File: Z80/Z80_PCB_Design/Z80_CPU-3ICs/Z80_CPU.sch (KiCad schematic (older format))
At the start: 47 parts, among them J1 USB_B, J2 Conn_01x12, J3 Conn_01x12, J4 Conn_01x02, U1 Z80CPU, U2 AS6C4008, U3 4.9152 MHz, U4 CY8C5267AXI-LP051, U5 MCP23017_SP, Y1 32.768KHz

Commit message: Added SPI pinout
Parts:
- MTG1, MTG2, MTG3, MTG4: symbol LandBoards:MTG_HOLE -> Z80_CPU-rescue:MTG_HOLE-LandBoards
- U3: symbol LandBoards_Semis:OSC -> Z80_CPU-rescue:OSC-LandBoards_Semis
- U4: symbol LandBoards_Semis:CY8C5888AXI-LP096 -> Z80_CPU-rescue:CY8C5888AXI-LP096-LandBoards_Semis
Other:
- note added: "AUDIO CONNECTOR/\nLOW PASS FILTER"
- note added: "TX (MISO)\nRX (MOSI)\nRTS (SCK)\nCTS (SS)"
- note removed: "AUDIO CONNECTOR"
- moved on the sheet: H3, J1, J2, J3, U1, U2, U5

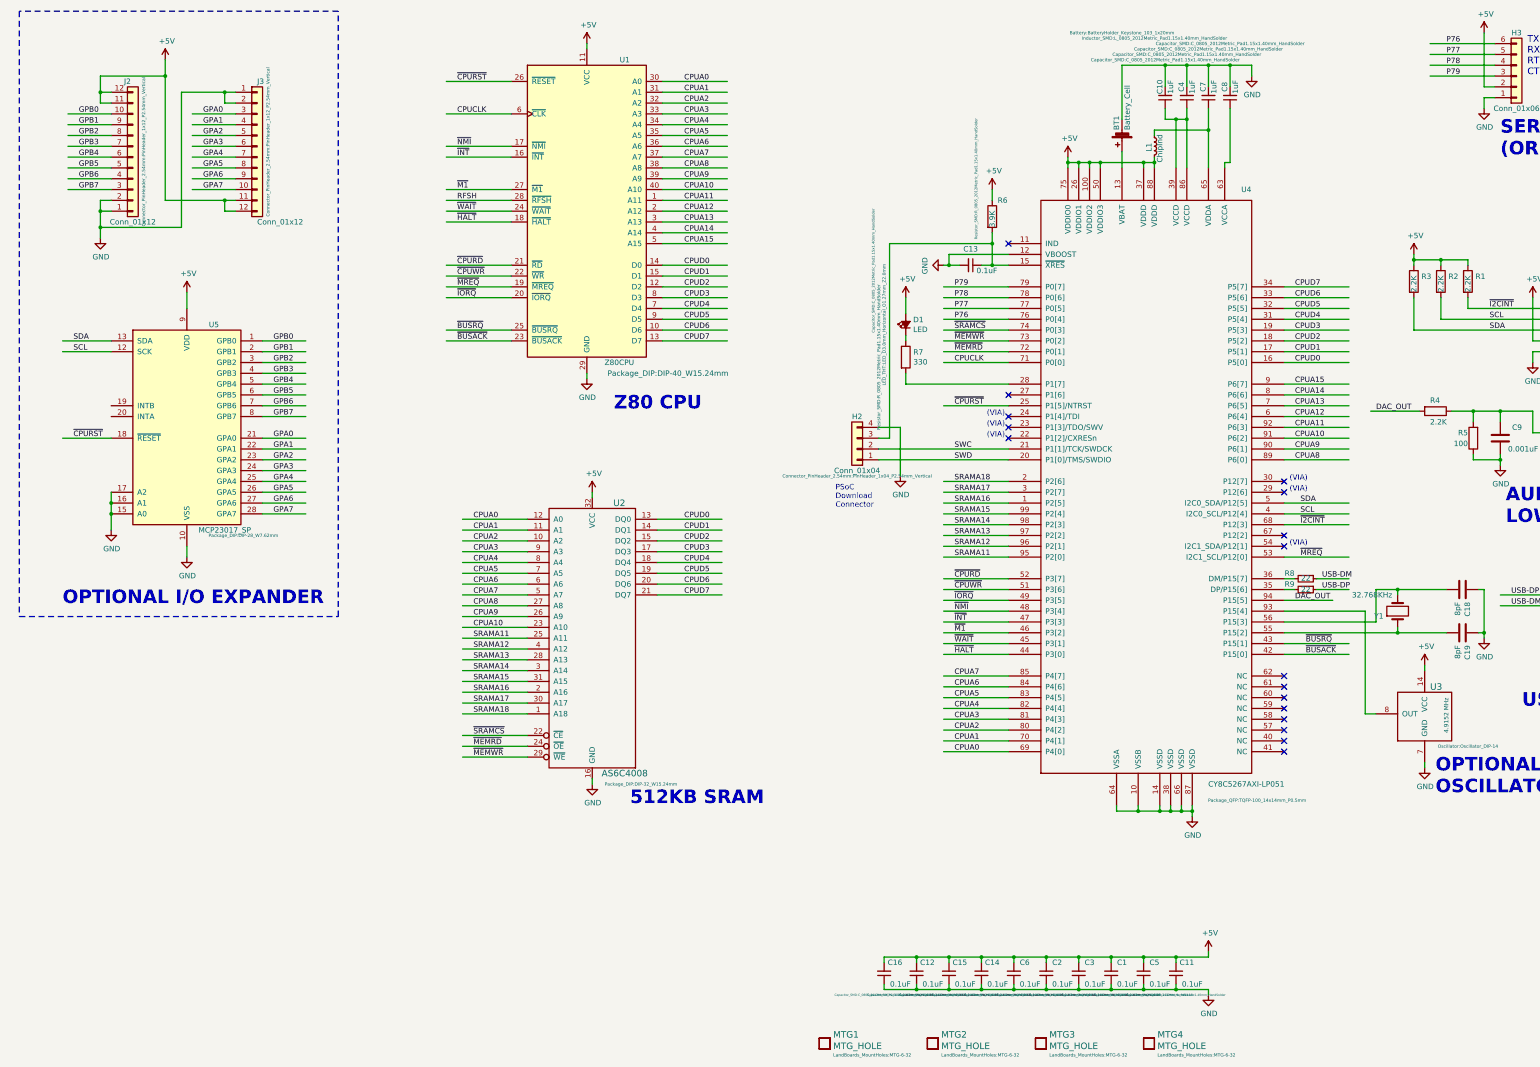
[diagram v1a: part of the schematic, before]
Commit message: Grand Piano on DAC8 output
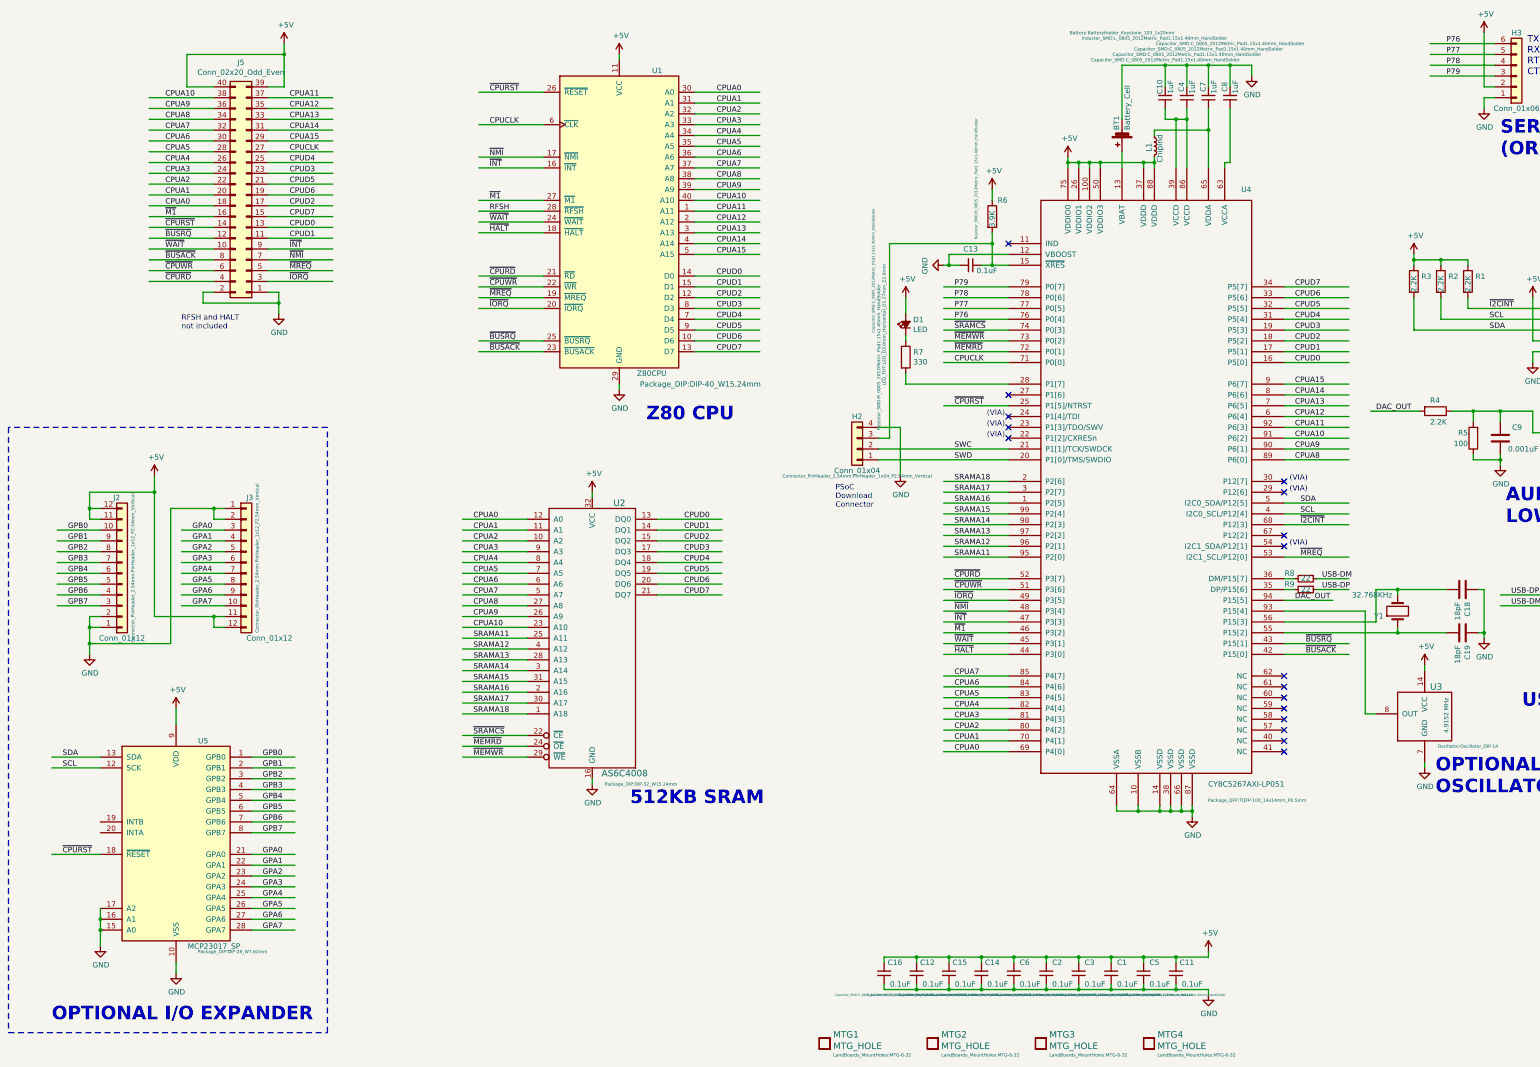
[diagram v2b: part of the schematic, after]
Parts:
- added J5: Conn_02x20_Odd_Even, Connector_PinHeader_2.54mm:PinHeader_2x20_P2.54mm_Horizontal, symbol Connector_Generic:Conn_02x20_Odd_Even
- C18, C19: value 8pF -> 18pF
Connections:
- wire segments 366 -> 414
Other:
- note added: "RFSH and HALT\nnot included"
- moved on the sheet: J2, J3, U1, U5

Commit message: pio init stuck z80
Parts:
- R1: value 2.2K -> 10K
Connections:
- wire segments 414 -> 418
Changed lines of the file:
@@
 P 14150 3300
 F 0 "R1" H 14220 3346 50  0000 L CNN
-F 1 "2.2K" V 14150 3200 50  0000 L CNN
+F 1 "10K" V 14150 3200 50  0000 L CNN
 F 2 "Resistor_SMD:R_0805_2012Metric_Pad1.15x1.40mm_HandSolder" V 14080 3300 50  0001 C CNN
 F 3 "~" H 14150 3300 50  0001 C CNN
@@
 Wire Wire Line
 	1950 1700 2550 1700
+Text Label 1150 8400 0    50   ~ 0
+~I2CINT
+Wire Wire Line
+	1050 8400 1450 8400
+Wire Wire Line
+	1450 8400 1450 8300
+Wire Wire Line
+	1450 8300 1500 8300
+Connection ~ 1450 8400
+Wire Wire Line
+	1450 8400 1500 8400
 $EndSCHEMATC

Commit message: remove cpu reset from expansion mcp23017
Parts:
- added R10: 10K, Resistor_SMD:R_0805_2012Metric_Pad1.15x1.40mm_HandSolder, symbol Device:R
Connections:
- wire segments 418 -> 420
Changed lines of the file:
@@
 	1    0    0    -1
 $EndComp
-Text Label 1150 8600 0    50   ~ 0
-~CPURST
-Wire Wire Line
-	1050 8600 1500 8600
+Wire Wire Line
+	850  8600 1500 8600
 Wire Wire Line
 	1500 9100 1500 9200
@@
 Wire Wire Line
 	1450 8400 1500 8400
+$Comp
+L Device:R R10
+U 1 1 5DC2CA82
+P 850 8350
+F 0 "R10" H 900 8500 50  0000 L CNN
+F 1 "10K" V 850 8250 50  0000 L CNN
+F 2 "Resistor_SMD:R_0805_2012Metric_Pad1.15x1.40mm_HandSolder" V 700 8700 25  0000 C CNN
+F 3 "~" H 850 8350 50  0001 C CNN
+	1    850  8350
+	1    0    0    -1
+$EndComp
+$Comp
+L power:+5V #PWR04
+U 1 1 5DC6B53D
+P 850 8050
+F 0 "#PWR04" H 850 7900 50  0001 C CNN
+F 1 "+5V" H 865 8223 50  0000 C CNN
+F 2 "" H 850 8050 50  0001 C CNN
+F 3 "" H 850 8050 50  0001 C CNN
+	1    850  8050
+	1    0    0    -1
+$EndComp
+Wire Wire Line
+	850  8050 850  8200
+Wire Wire Line
+	850  8500 850  8600
 $EndSCHEMATC

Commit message: Add 4 pin connector to spare PSoC pins
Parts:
- added H4: Conn_01x06, Connector_PinHeader_2.54mm:PinHeader_1x06_P2.54mm_Vertical, symbol Connector_Generic:Conn_01x06
- L1: value ChipInd -> HZ0805E601R-10
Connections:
- net labels added: P22, P23, P24, P27
- wire segments 420 -> 432
- no-connect marks 17 -> 13
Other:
- note added: "GND\n~RST\nSWC\nSWD"
- moved on the sheet: H1, J1, R1, R2, R3, Y1
